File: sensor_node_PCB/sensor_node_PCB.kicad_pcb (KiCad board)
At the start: 2 copper layers, 102.6 x 47.7 mm, 51 parts, among them J1 USB_B_Mini, J2 INPUT CONNECTOR, J3 OUTPUT_CONNECTOR, P1 BREAKOUTS, Q1 FDN340P, Q2 BSS138, Q3 BSS138, SW1 RESET_SWITCH, U1 LMV358IDGKR, U2 LD1117S50TR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

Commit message: made 12v bus line bigger and moved away from bme280
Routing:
- net 12V_BUS: track 135.2 -> 142.3 mm
- net GND: vias 10 -> 11
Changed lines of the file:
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@@
   (general
     (thickness 1.6)
-    (drawings 13)
-    (tracks 488)
+    (drawings 16)
+    (tracks 487)
     (zones 0)
     (modules 51)
@@
     (38 B.Mask user hide)
     (39 F.Mask user hide)
-    (40 Dwgs.User user hide)
+    (40 Dwgs.User user)
     (41 Cmts.User user)
     (42 Eco1.User user hide)
@@
   )
   (setup
-    (last_trace_width 0.127)
+    (last_trace_width 0.5)
     (user_trace_width 0.127)
+    (user_trace_width 0.5)
     (trace_clearance 0.2)
     (zone_clearance 0.254)
@@
       (rotate (xyz 0 0 0))
     )
+  )
+  (dimension 102.746846 (width 0.15) (layer Dwgs.User)
+    (gr_text "102.747 mm" (at 148.930159 76.239143 359.5042516) (layer Dwgs.User)
+      (effects (font (size 1 1) (thickness 0.15)))
+    )
+    (feature1 (pts (xy 200.152 93.98) (xy 200.295485 77.397195)))
+    (feature2 (pts (xy 97.409 93.091) (xy 97.552485 76.508195)))
+    (crossbar (pts (xy 97.547411 77.094594) (xy 200.290411 77.983594)))
+    (arrow1a (pts (xy 200.290411 77.983594) (xy 199.158876 78.560246)))
+    (arrow1b (pts (xy 200.290411 77.983594) (xy 199.169023 77.387448)))
+    (arrow2a (pts (xy 97.547411 77.094594) (xy 98.668799 77.69074)))
+    (arrow2b (pts (xy 97.547411 77.094594) (xy 98.678946 76.517942)))
+  )
+  (dimension 36.957218 (width 0.15) (layer Dwgs.User)
+    (gr_text "36.957 mm" (at 87.540192 108.454817 270.1968919) (layer Dwgs.User)
+      (effects (font (size 1 1) (thickness 0.15)))
+    )
+    (feature1 (pts (xy 105.156 126.873) (xy 88.317267 126.930865)))
+    (feature2 (pts (xy 105.029 89.916) (xy 88.190267 89.973865)))
+    (crossbar (pts (xy 88.776684 89.97185) (xy 88.903684 126.92885)))
+    (arrow1a (pts (xy 88.903684 126.92885) (xy 88.313396 125.804368)))
+    (arrow1b (pts (xy 88.903684 126.92885) (xy 89.48623 125.800338)))
+    (arrow2a (pts (xy 88.776684 89.97185) (xy 88.194138 91.100362)))
+    (arrow2b (pts (xy 88.776684 89.97185) (xy 89.366972 91.096332)))
+  )
+  (dimension 1.909229 (width 0.12) (layer F.SilkS)
+    (gr_text "1.909 mm" (at 101.907198 63.154968 3.814074834) (layer F.SilkS)
+      (effects (font (size 1 1) (thickness 0.15)))
+    )
+    (feature1 (pts (xy 104.648 89.916) (xy 102.905169 63.773533)))
+    (feature2 (pts (xy 102.743 90.043) (xy 101.000169 63.900533)))
+    (crossbar (pts (xy 101.039177 64.485655) (xy 102.944177 64.358655)))
+    (arrow1a (pts (xy 102.944177 64.358655) (xy 101.859176 65.018711)))
+    (arrow1b (pts (xy 102.944177 64.358655) (xy 101.78116 63.848467)))
+    (arrow2a (pts (xy 101.039177 64.485655) (xy 102.202194 64.995843)))
+    (arrow2b (pts (xy 101.039177 64.485655) (xy 102.124178 63.825599)))
   )
   (gr_line (start 115.541438 126.960848) (end 185.38 126.96) (layer Edge.Cuts) (width 0.05))
@@
   (segment (start 147.54 91.8) (end 147.54 93.355634) (width 0.127) (layer F.Cu) (net 2))
   (segment (start 147.169634 93.726) (end 147.066 93.726) (width 0.127) (layer F.Cu) (net 2))
+  (via (at 146.685 108.204) (size 0.45) (drill 0.2) (layers F.Cu B.Cu) (net 2))
   (segment (start 116.9625 112.8) (end 117.4 112.8) (width 0.127) (layer F.Cu) (net 3))
   (segment (start 116.8 112.8) (end 116.9625 112.8) (width 0.127) (layer F.Cu) (net 3))
@@
   (segment (start 141.275 108.7) (end 143.8 108.7) (width 0.127) (layer F.Cu) (net 9))
   (segment (start 103.84 116.94) (end 103.9 117) (width 0.127) (layer F.Cu) (net 10))
-  (segment (start 190.373 116.205) (end 190.373 102.489) (width 0.25) (layer B.Cu) (net 10))
-  (segment (start 184.785 121.793) (end 190.373 116.205) (width 0.25) (layer B.Cu) (net 10))
-  (segment (start 104.1 117.53) (end 110.141 123.571) (width 0.25) (layer B.Cu) (net 10))
-  (segment (start 190.373 102.489) (end 192.278 100.584) (width 0.25) (layer B.Cu) (net 10))
-  (segment (start 110.141 123.571) (end 166.497 123.571) (width 0.25) (layer B.Cu) (net 10))
-  (segment (start 166.497 123.571) (end 168.275 121.793) (width 0.25) (layer B.Cu) (net 10))
-  (segment (start 192.278 100.584) (end 194.437 100.584) (width 0.25) (layer B.Cu) (net 10))
-  (segment (start 104.1 116.24) (end 104.1 117.53) (width 0.25) (layer B.Cu) (net 10))
-  (segment (start 168.275 121.793) (end 184.785 121.793) (width 0.25) (layer B.Cu) (net 10))
   (segment (start 106.15 116.24) (end 107.823 114.567) (width 0.25) (layer F.Cu) (net 10))
   (segment (start 104.1 116.24) (end 106.15 116.24) (width 0.25) (layer F.Cu) (net 10))
@@
   (segment (start 107.823 101.473) (end 110.744 98.552) (width 0.25) (layer F.Cu) (net 10))
   (segment (start 110.744 98.552) (end 112.522 98.552) (width 0.25) (layer F.Cu) (net 10))
+  (segment (start 101.8 116.24) (end 100.076 114.516) (width 0.5) (layer B.Cu) (net 10))
+  (segment (start 104.1 116.24) (end 101.8 116.24) (width 0.5) (layer B.Cu) (net 10))
+  (segment (start 100.076 114.516) (end 100.076 98.425) (width 0.5) (layer B.Cu) (net 10))
+  (segment (start 100.076 98.425) (end 101.473 97.028) (width 0.5) (layer B.Cu) (net 10))
+  (segment (start 101.473 97.028) (end 192.913 97.028) (width 0.5) (layer B.Cu) (net 10))
+  (segment (start 192.913 97.028) (end 194.691 98.806) (width 0.5) (layer B.Cu) (net 10))
+  (segment (start 194.691 98.806) (end 194.691 100.838) (width 0.5) (layer B.Cu) (net 10))
   (segment (start 113.2 94.6) (end 116.952 94.6) (width 0.127) (layer F.Cu) (net 11))
   (segment (start 116.952 94.6) (end 117.094 94.742) (width 0.127) (layer F.Cu) (net 11))

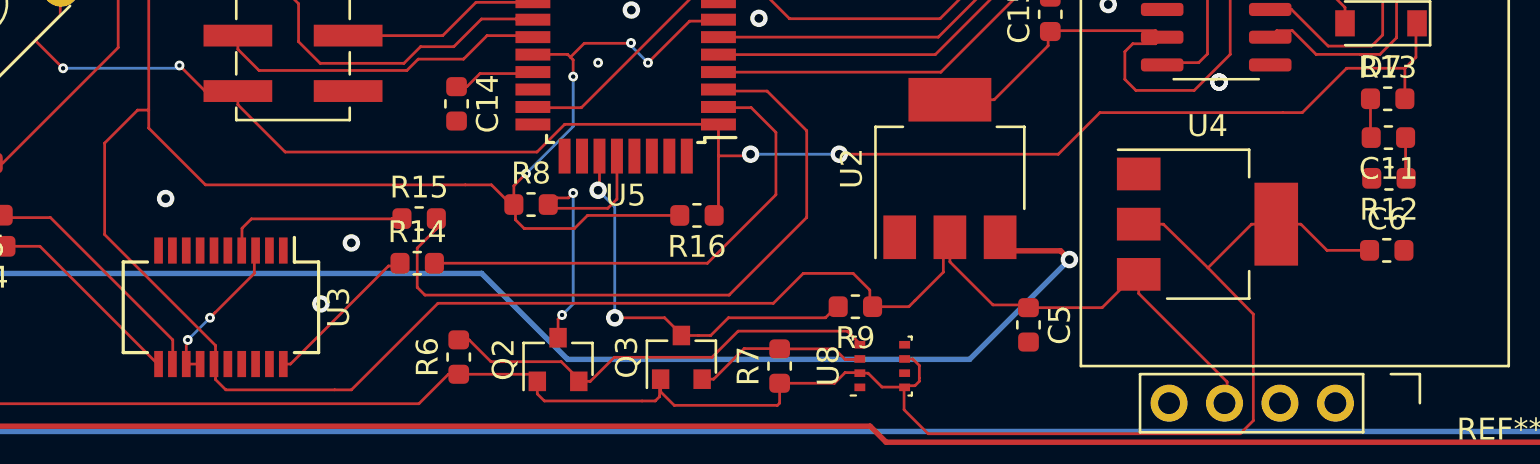
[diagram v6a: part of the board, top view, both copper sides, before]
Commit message: added missing dtr trace
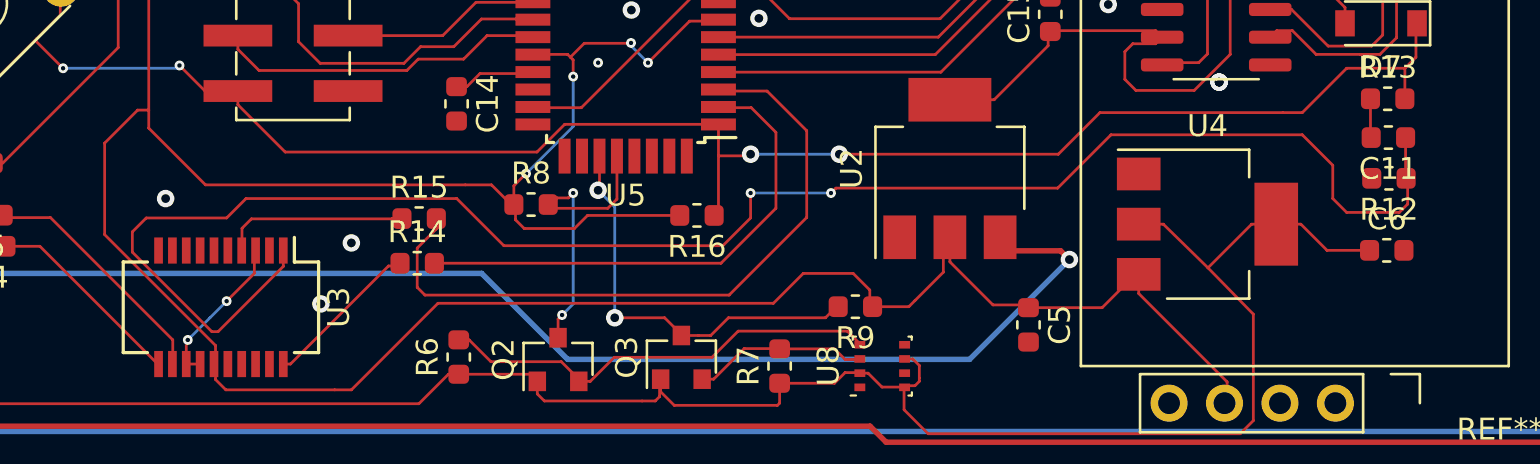
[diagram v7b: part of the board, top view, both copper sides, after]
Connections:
- C11 pad 1: /atmega328p/DTR -> /ard_DTR
- R12 pad 1: /atmega328p/DTR -> /ard_DTR
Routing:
- net /ard_DTR: track 0.00 -> 79.6 mm, vias 0 -> 2
- net /atmega328p/DTR: track 1.92 -> 0.00 mm

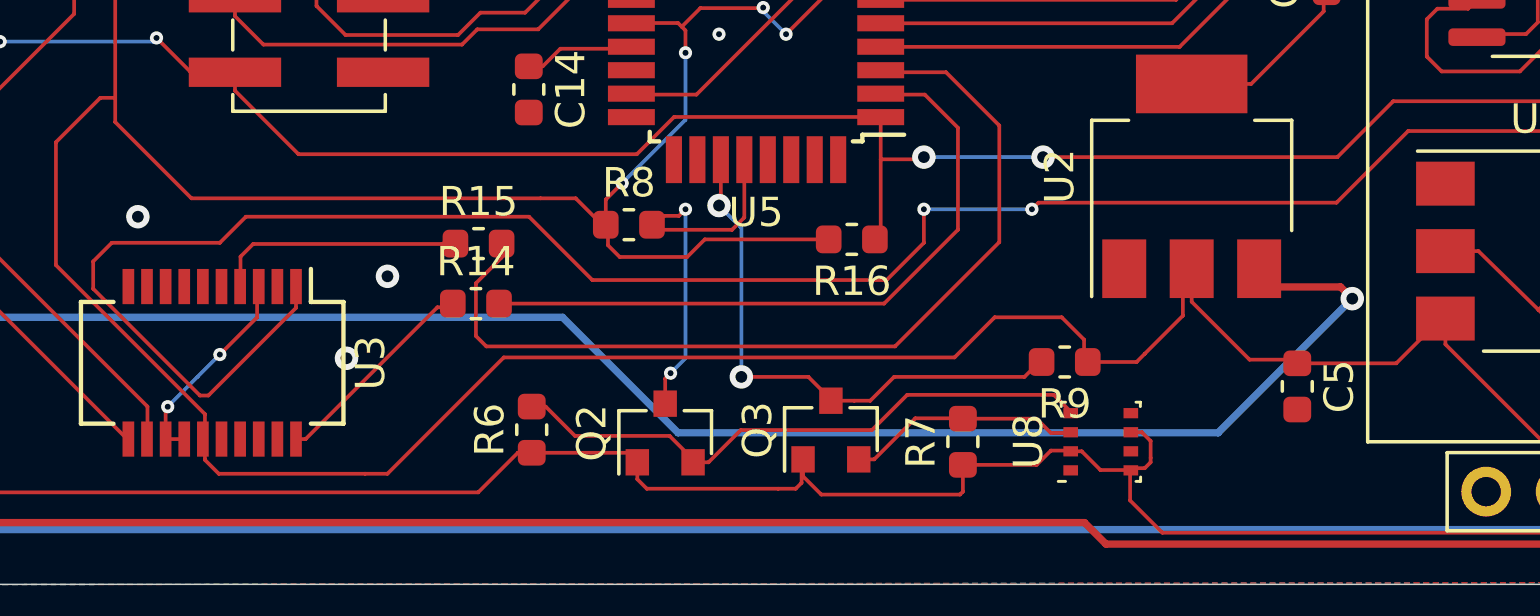
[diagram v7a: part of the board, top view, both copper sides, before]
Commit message: moved vin trace away from bme280
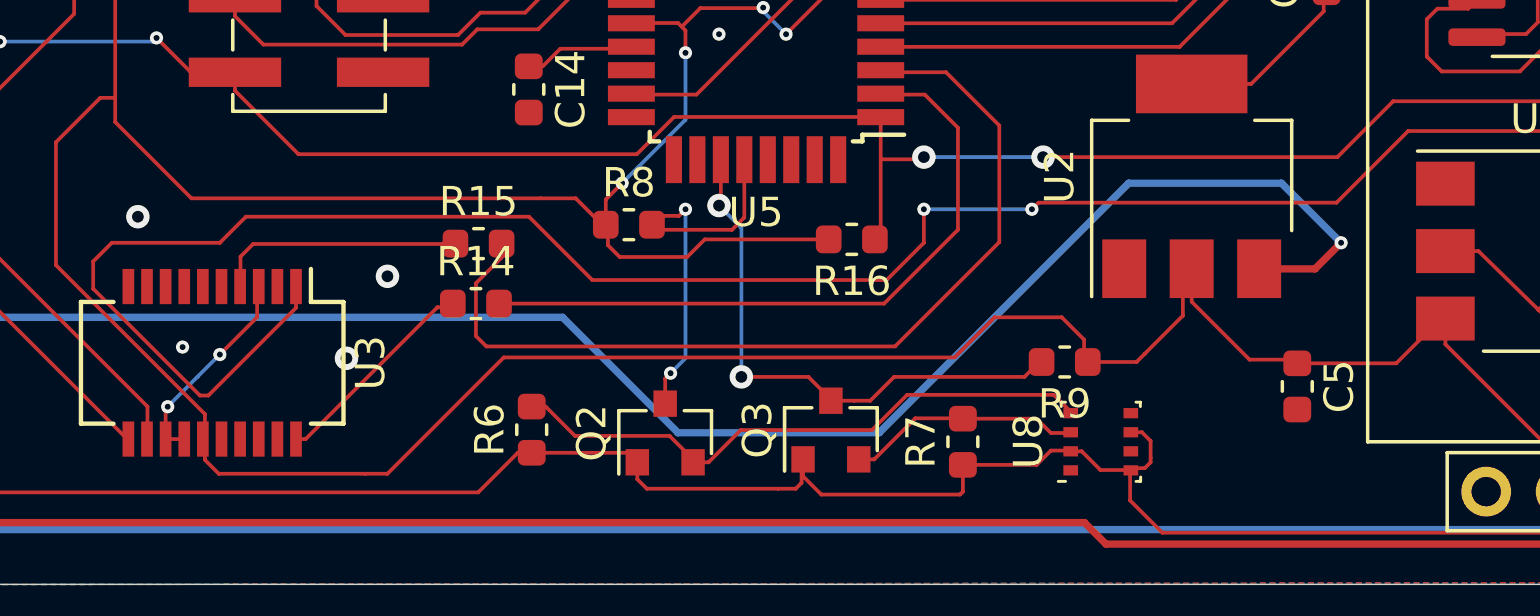
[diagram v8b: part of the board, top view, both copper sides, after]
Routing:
- net Vin: track 102.1 -> 104.7 mm
- net GND: vias 11 -> 12
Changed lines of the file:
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@@
     (thickness 1.6)
     (drawings 16)
-    (tracks 513)
+    (tracks 516)
     (zones 0)
     (modules 51)
@@
   )
   (setup
-    (last_trace_width 0.127)
+    (last_trace_width 0.25)
     (user_trace_width 0.127)
     (user_trace_width 0.5)
@@
   (segment (start 147.169634 93.726) (end 147.066 93.726) (width 0.127) (layer F.Cu) (net 2))
   (via (at 146.685 108.204) (size 0.45) (drill 0.2) (layers F.Cu B.Cu) (net 2))
+  (via (at 128.397 118.872) (size 0.45) (drill 0.2) (layers F.Cu B.Cu) (net 2))
   (segment (start 116.9625 112.8) (end 117.4 112.8) (width 0.127) (layer F.Cu) (net 3))
   (segment (start 116.8 112.8) (end 116.9625 112.8) (width 0.127) (layer F.Cu) (net 3))
@@
   (segment (start 110.998 117.856) (end 141.351 117.856) (width 0.25) (layer B.Cu) (net 3))
   (segment (start 141.351 117.856) (end 145.288 121.793) (width 0.25) (layer B.Cu) (net 3))
-  (via (at 168.275 117.221) (size 0.8) (drill 0.4) (layers F.Cu B.Cu) (net 3))
-  (segment (start 145.288 121.793) (end 163.703 121.793) (width 0.25) (layer B.Cu) (net 3))
-  (segment (start 163.703 121.793) (end 168.275 117.221) (width 0.25) (layer B.Cu) (net 3))
-  (segment (start 167.875001 116.821001) (end 165.843001 116.821001) (width 0.25) (layer F.Cu) (net 3))
-  (segment (start 168.275 117.221) (end 167.875001 116.821001) (width 0.25) (layer F.Cu) (net 3))
+  (segment (start 145.288 121.793) (end 152.146 121.793) (width 0.25) (layer B.Cu) (net 3))
+  (segment (start 152.146 121.793) (end 160.655 113.284) (width 0.25) (layer B.Cu) (net 3))
+  (via (at 167.894 115.316) (size 0.45) (drill 0.2) (layers F.Cu B.Cu) (net 3))
+  (segment (start 160.655 113.284) (end 165.862 113.284) (width 0.25) (layer B.Cu) (net 3))
+  (segment (start 165.862 113.284) (end 167.894 115.316) (width 0.25) (layer B.Cu) (net 3))
+  (segment (start 167.894 115.316) (end 167.005 116.205) (width 0.25) (layer F.Cu) (net 3))
+  (segment (start 167.005 116.205) (end 165.1 116.205) (width 0.25) (layer F.Cu) (net 3))
   (segment (start 140.3 122.475) (end 143.575 122.475) (width 0.127) (layer F.Cu) (net 4))
   (segment (start 143.575 122.475) (end 143.9 122.8) (width 0.127) (layer F.Cu) (net 4))
@@
   (via (at 157.734 112.395) (size 0.8) (drill 0.4) (layers F.Cu B.Cu) (net 11))
   (segment (start 153.67 112.395) (end 157.734 112.395) (width 0.127) (layer B.Cu) (net 11))
-  (segment (start 157.734 112.395) (end 167.767 112.395) (width 0.127) (layer F.Cu) (net 11))
-  (segment (start 167.767 112.395) (end 169.672 110.49) (width 0.127) (layer F.Cu) (net 11))
-  (segment (start 169.672 110.49) (end 178.054 110.49) (width 0.127) (layer F.Cu) (net 11))
-  (segment (start 178.054 110.49) (end 178.943 110.49) (width 0.127) (layer F.Cu) (net 11))
-  (segment (start 178.943 110.49) (end 180.975 108.458) (width 0.127) (layer F.Cu) (net 11))
-  (segment (start 180.975 108.458) (end 183.642 108.458) (width 0.127) (layer F.Cu) (net 11))
   (segment (start 183.642 108.458) (end 184.15 107.95) (width 0.127) (layer F.Cu) (net 11))
   (segment (start 184.15 107.95) (end 184.15 106.553) (width 0.127) (layer F.Cu) (net 11))
@@
   (segment (start 127.508 108.331) (end 128.651 109.474) (width 0.127) (layer F.Cu) (net 11))
   (segment (start 128.651 109.474) (end 130.175 109.474) (width 0.127) (layer F.Cu) (net 11))
+  (segment (start 178.054 110.49) (end 178.943 110.49) (width 0.127) (layer F.Cu) (net 11))
+  (segment (start 178.943 110.49) (end 180.975 108.458) (width 0.127) (layer F.Cu) (net 11))
+  (segment (start 180.975 108.458) (end 183.642 108.458) (width 0.127) (layer F.Cu) (net 11))
+  (segment (start 169.672 110.49) (end 178.054 110.49) (width 0.127) (layer F.Cu) (net 11))
+  (segment (start 167.767 112.395) (end 169.672 110.49) (width 0.127) (layer F.Cu) (net 11))
+  (segment (start 157.734 112.395) (end 167.767 112.395) (width 0.127) (layer F.Cu) (net 11))
   (segment (start 113.275 111.1) (end 124.1 100.275) (width 0.127) (layer F.Cu) (net 12))
   (segment (start 112.4 111.1) (end 113.275 111.1) (width 0.127) (layer F.Cu) (net 12))
@@
   (segment (start 198.628 106.68) (end 197.612 105.664) (width 0.25) (layer B.Cu) (net 20))
   (segment (start 197.612 105.664) (end 194.691 105.664) (width 0.25) (layer B.Cu) (net 20))
+  (segment (start 177.475 107.035) (end 177.775 106.735) (width 0.127) (layer F.Cu) (net 20))
+  (segment (start 182.499 107.823) (end 183.261 107.061) (width 0.127) (layer F.Cu) (net 20))
+  (segment (start 181.61 107.823) (end 182.499 107.823) (width 0.127) (layer F.Cu) (net 20))
+  (segment (start 179.578 107.823) (end 181.61 107.823) (width 0.127) (layer F.Cu) (net 20))
+  (segment (start 178.49 106.735) (end 179.578 107.823) (width 0.127) (layer F.Cu) (net 20))
   (segment (start 177.775 106.735) (end 178.49 106.735) (width 0.127) (layer F.Cu) (net 20))
-  (segment (start 177.475 107.035) (end 177.775 106.735) (width 0.127) (layer F.Cu) (net 20))
-  (segment (start 178.49 106.735) (end 179.578 107.823) (width 0.127) (layer F.Cu) (net 20))
-  (segment (start 179.578 107.823) (end 181.61 107.823) (width 0.127) (layer F.Cu) (net 20))
-  (segment (start 181.61 107.823) (end 182.499 107.823) (width 0.127) (layer F.Cu) (net 20))
-  (segment (start 182.499 107.823) (end 183.261 107.061) (width 0.127) (layer F.Cu) (net 20))
   (segment (start 183.261 107.061) (end 183.261 105.156) (width 0.127) (layer F.Cu) (net 20))
   (segment (start 183.261 105.156) (end 184.023 104.394) (width 0.127) (layer F.Cu) (net 20))
@@
   (segment (start 198.374 112.776) (end 196.469 110.871) (width 0.25) (layer F.Cu) (net 21))
   (segment (start 196.469 110.871) (end 194.564 110.871) (width 0.25) (layer F.Cu) (net 21))
+  (segment (start 180.127 107.442) (end 182.118 107.442) (width 0.127) (layer F.Cu) (net 21))
   (segment (start 178.45 105.765) (end 180.127 107.442) (width 0.127) (layer F.Cu) (net 21))
+  (segment (start 182.118 107.442) (end 182.626 106.934) (width 0.127) (layer F.Cu) (net 21))
   (segment (start 177.475 105.765) (end 178.45 105.765) (width 0.127) (layer F.Cu) (net 21))
-  (segment (start 180.127 107.442) (end 182.118 107.442) (width 0.127) (layer F.Cu) (net 21))
-  (segment (start 182.118 107.442) (end 182.626 106.934) (width 0.127) (layer F.Cu) (net 21))
+  (segment (start 182.626 104.394) (end 184.023 102.997) (width 0.127) (layer F.Cu) (net 21))
+  (segment (start 198.12 107.188) (end 194.564 110.744) (width 0.127) (layer F.Cu) (net 21))
   (segment (start 182.626 106.934) (end 182.626 104.394) (width 0.127) (layer F.Cu) (net 21))
-  (segment (start 182.626 104.394) (end 184.023 102.997) (width 0.127) (layer F.Cu) (net 21))
   (segment (start 184.023 102.997) (end 196.723 102.997) (width 0.127) (layer F.Cu) (net 21))
   (segment (start 196.723 102.997) (end 198.12 104.394) (width 0.127) (layer F.Cu) (net 21))
   (segment (start 198.12 104.394) (end 198.12 107.188) (width 0.127) (layer F.Cu) (net 21))
-  (segment (start 198.12 107.188) (end 194.564 110.744) (width 0.127) (layer F.Cu) (net 21))
   (segment (start 146.7669 102.1995) (end 146.7669 103.9902) (width 0.127) (layer F.Cu) (net 22))
   (segment (start 146.7669 95.1131) (end 146.7669 102.1995) (width 0.127) (layer F.Cu) (net 22))
@@
   (segment (start 148.35 100.165634) (end 148.35 103.82) (width 0.127) (layer F.Cu) (net 24))
   (segment (start 148.35 103.82) (end 148.35 104) (width 0.127) (layer F.Cu) (net 24))
+  (segment (start 145.916 110.264) (end 143.5411 110.264) (width 0.127) (layer F.Cu) (net 25))
+  (segment (start 155.4537 106.1873) (end 153.282 104.0156) (width 0.127) (layer F.Cu) (net 25))
   (segment (start 165.5375 103.000038) (end 162.350238 106.1873) (width 0.127) (layer F.Cu) (net 25))
   (segment (start 161.234 91.8) (end 165.5375 96.1035) (width 0.127) (layer F.Cu) (net 25))
-  (segment (start 155.4537 106.1873) (end 153.282 104.0156) (width 0.127) (layer F.Cu) (net 25))
-  (segment (start 157.7 91.8) (end 161.234 91.8) (width 0.127) (layer F.Cu) (net 25))
-  (segment (start 153.282 104.0156) (end 152.1644 104.0156) (width 0.127) (layer F.Cu) (net 25))
-  (segment (start 145.916 110.264) (end 143.5411 110.264) (width 0.127) (layer F.Cu) (net 25))
   (segment (start 152.1644 104.0156) (end 145.916 110.264) (width 0.127) (layer F.Cu) (net 25))
   (segment (start 162.350238 106.1873) (end 155.4537 106.1873) (width 0.127) (layer F.Cu) (net 25))
   (segment (start 165.5375 96.1035) (end 165.5375 103.000038) (width 0.127) (layer F.Cu) (net 25))
+  (segment (start 153.282 104.0156) (end 152.1644 104.0156) (width 0.127) (layer F.Cu) (net 25))
+  (segment (start 157.7 91.8) (end 161.234 91.8) (width 0.127) (layer F.Cu) (net 25))
   (segment (start 125.022 95.321) (end 127.712 95.321) (width 0.127) (layer F.Cu) (net 26))
   (segment (start 127.712 95.321) (end 128.517 94.516) (width 0.127) (layer F.Cu) (net 26))
@@
   (segment (start 128.905 119.888) (end 129.667 119.126) (width 0.127) (layer B.Cu) (net 40))
   (segment (start 129.667 119.126) (end 130.937 117.856) (width 0.127) (layer F.Cu) (net 40))
+  (segment (start 172.525 104.495) (end 166.529926 104.495) (width 0.127) (layer F.Cu) (net 49))
+  (segment (start 162.388427 108.636499) (end 152.036499 108.636499) (width 0.127) (layer F.Cu) (net 49))
   (segment (start 152.036499 108.636499) (end 152 108.6) (width 0.127) (layer F.Cu) (net 49))
-  (segment (start 162.388427 108.636499) (end 152.036499 108.636499) (width 0.127) (layer F.Cu) (net 49))
-  (segment (start 172.525 104.495) (end 166.529926 104.495) (width 0.127) (layer F.Cu) (net 49))
   (segment (start 166.529926 104.495) (end 162.388427 108.636499) (width 0.127) (layer F.Cu) (net 49))
   (segment (start 173.5 102.8) (end 174.6 103.9) (width 0.127) (layer F.Cu) (net 50))
